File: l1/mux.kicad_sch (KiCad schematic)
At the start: 38 parts, among them U202 CD74HC4067SM, U203 CD74HC4067SM

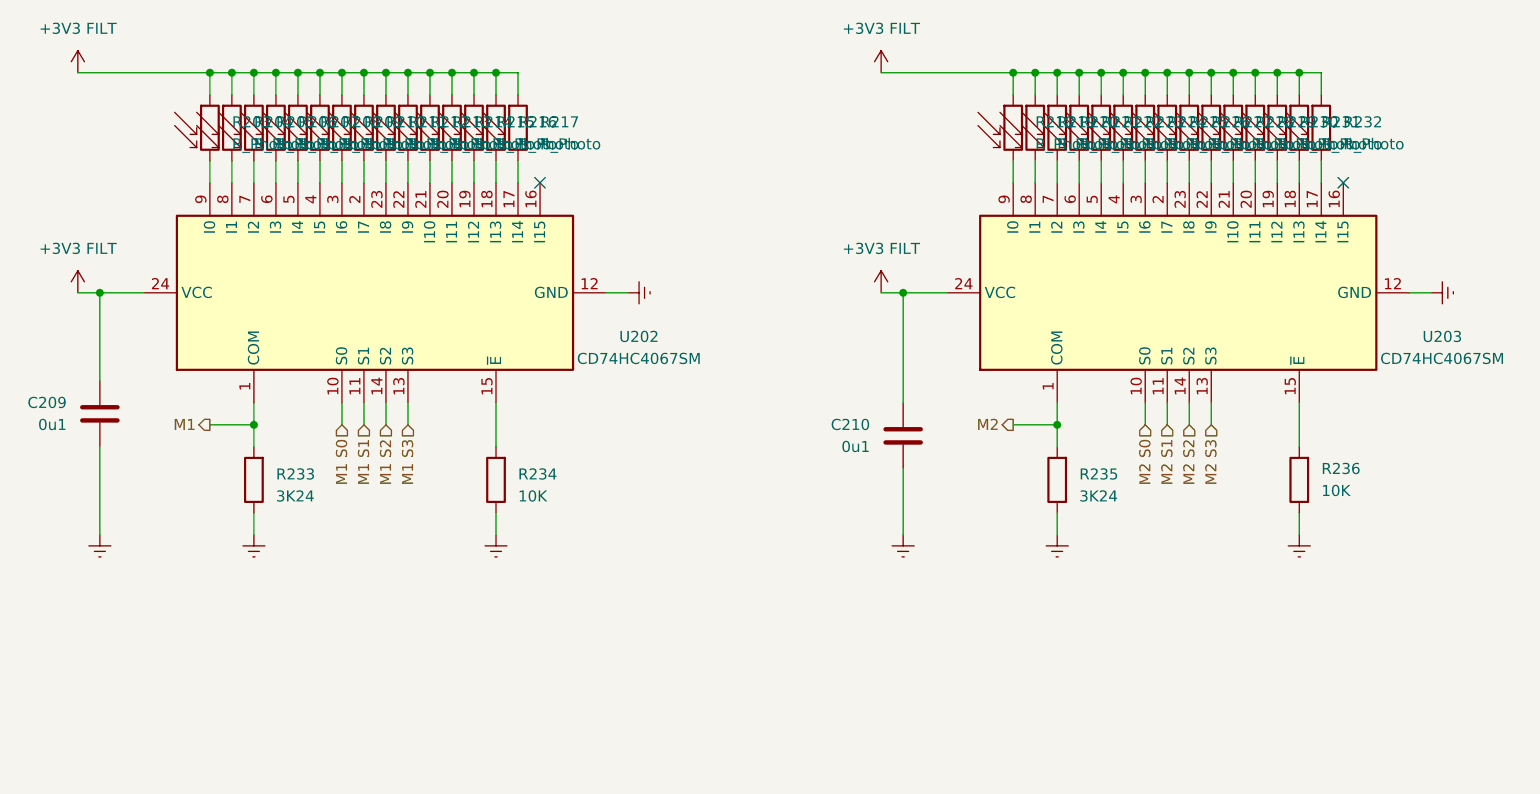
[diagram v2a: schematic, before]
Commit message: symbol designators
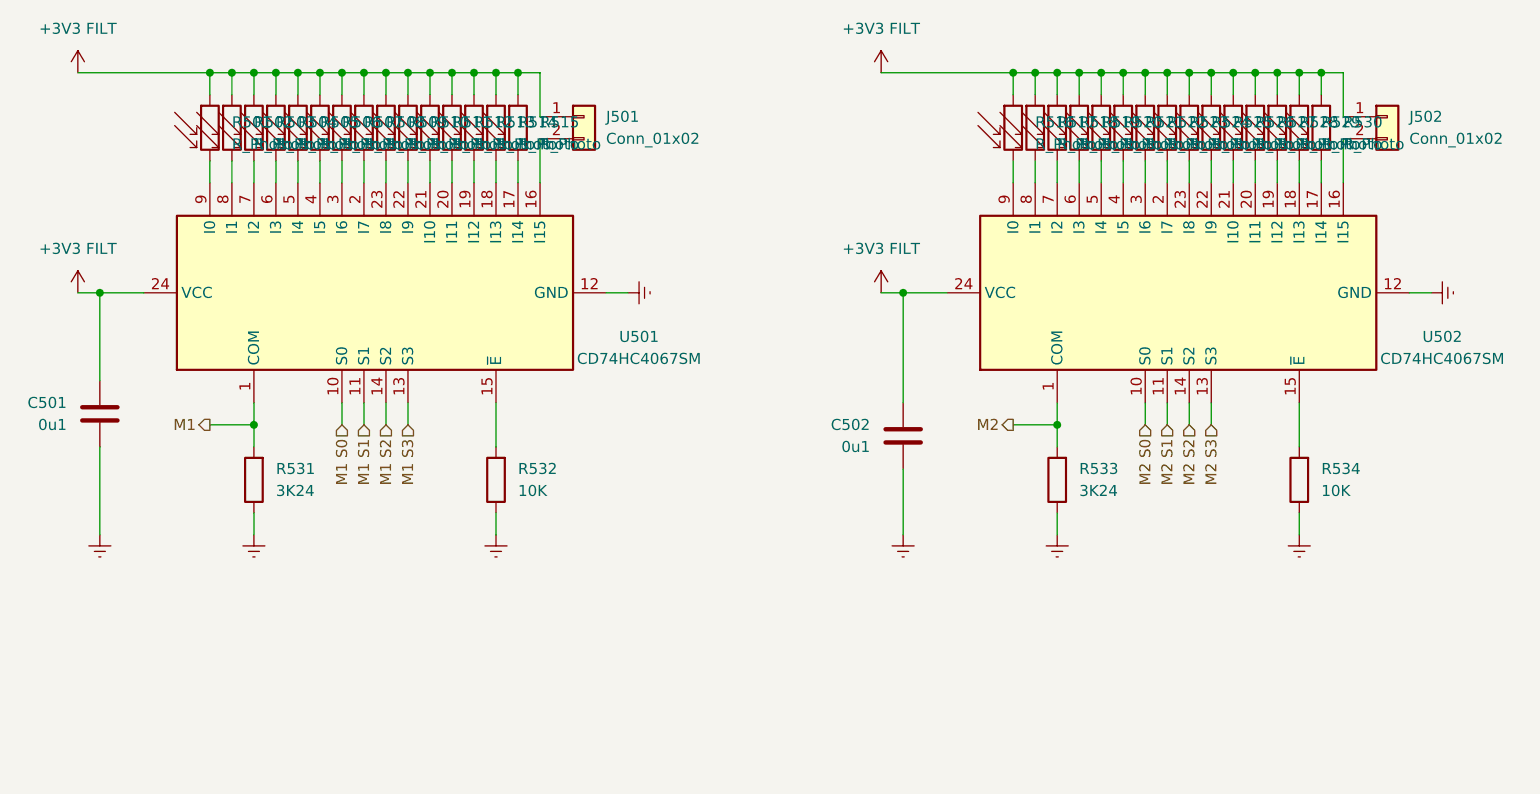
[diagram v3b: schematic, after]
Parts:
- added J501, J502: Conn_01x02, symbol Connector_Generic:Conn_01x02
- renumbered C209 to C501, C210 to C502, R203 to R501, R204 to R502, R205 to R503, R206 to R504, R207 to R505, R208 to R506, R209 to R507, R210 to R508, R211 to R509, R212 to R510, R213 to R511, R214 to R512, R215 to R513, R216 to R514, R217 to R515, R218 to R516, R219 to R517, R220 to R518, R221 to R519, R222 to R520, R223 to R521, R224 to R522, R225 to R523, R226 to R524, R227 to R525, R228 to R526, R229 to R527, R230 to R528, R231 to R529, R232 to R530, R233 to R531, R234 to R532, R235 to R533, R236 to R534, U202 to U501, U203 to U502
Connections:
- net +3V3 FILT: now also J501.1 (Pin_1), J502.1 (Pin_1)
- net at U501.16 (I15): now also J501.2 (Pin_2)
- net at U502.16 (I15): now also J502.2 (Pin_2)
- no-connect marks 2 -> 0

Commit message: Single STM32
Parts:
- added J503, J504: Conn_01x02, Connector_PinHeader_2.54mm:PinHeader_1x02_P2.54mm_Vertical, symbol Connector_Generic:Conn_01x02
- J501, J502: footprint (none) -> Connector_PinHeader_2.54mm:PinHeader_1x02_P2.54mm_Vertical
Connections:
- net +3V3 FILT: now also J503.1 (Pin_1), J504.1 (Pin_1)
- net GNDREF: now also J503.2 (Pin_2), J504.2 (Pin_2)
